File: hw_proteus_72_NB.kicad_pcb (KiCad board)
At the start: 2 copper layers, 154 x 159 mm, 130 parts, among them P1 1123038-2

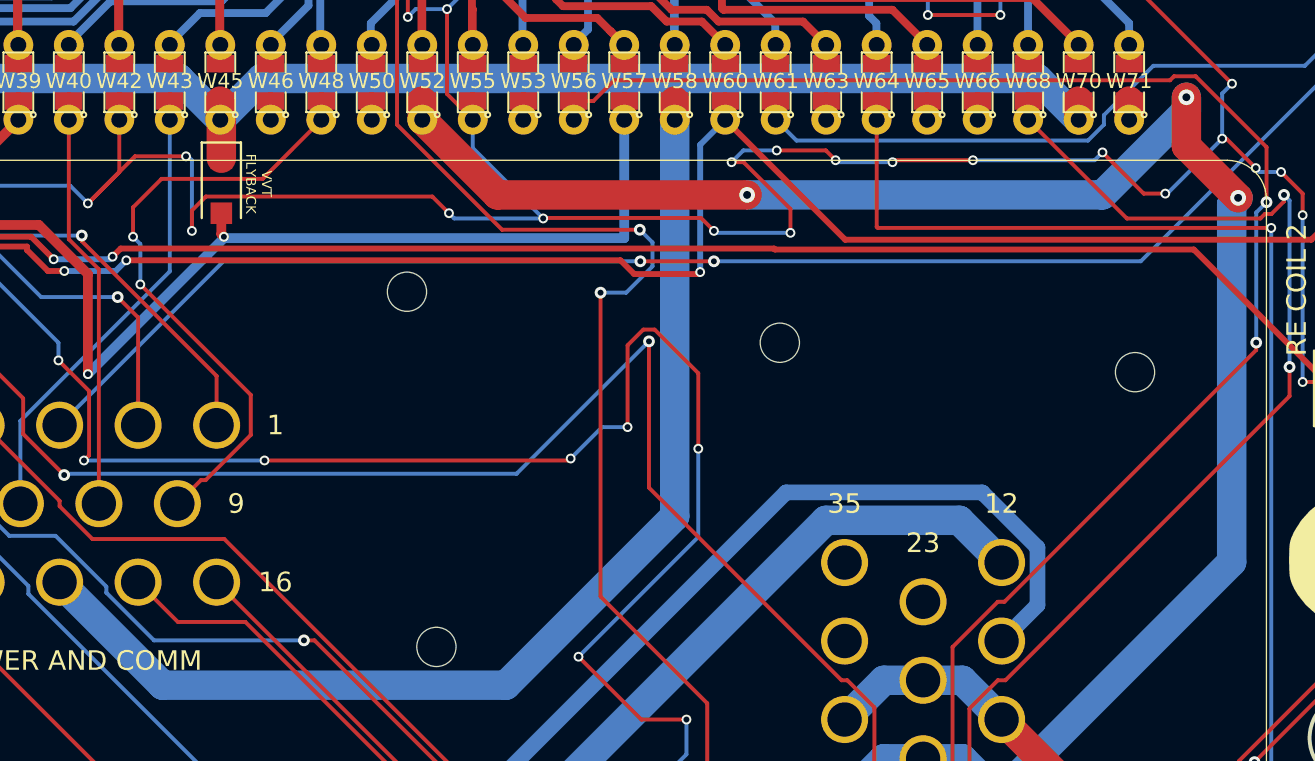
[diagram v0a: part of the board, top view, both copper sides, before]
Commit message: Added knock sensing connection
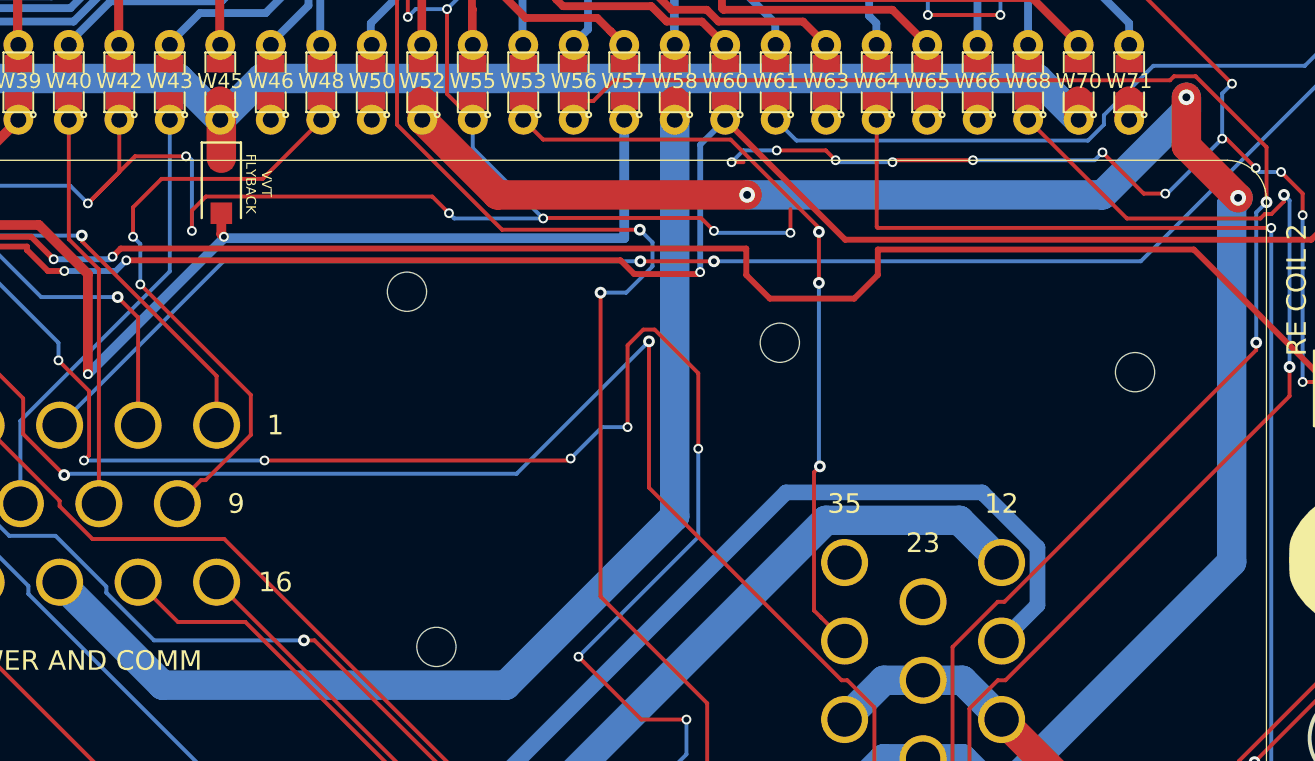
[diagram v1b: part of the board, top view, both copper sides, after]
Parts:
- renumbered e to D5
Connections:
- PROT2 pad 34: /KNOCK1 -> /KNOCK
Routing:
- net /KNOCK: track 0.95 -> 40.1 mm, vias 0 -> 3
- net /IGN4: track 266.7 -> 270.3 mm
- net GND: track 1283.1 -> 1279.7 mm

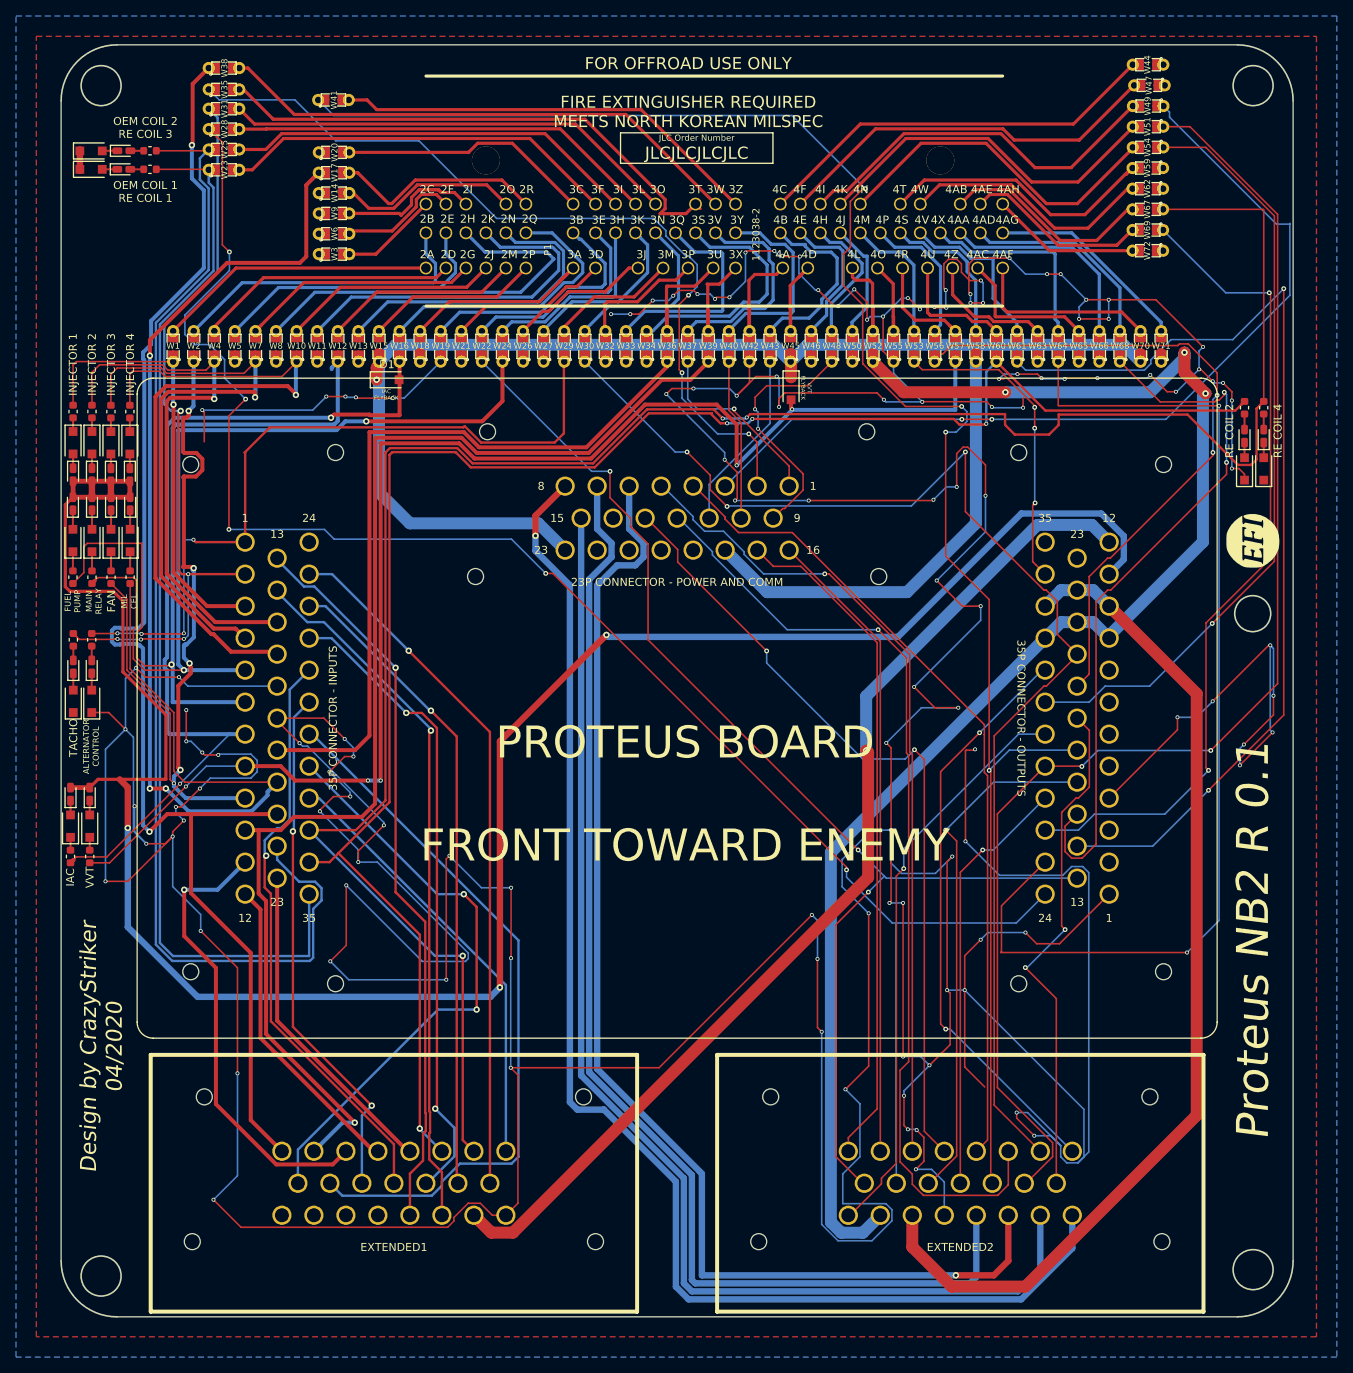
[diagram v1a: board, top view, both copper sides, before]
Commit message: Beefed up injector wires, as well as VVT and IAC low sides. Started the ground stitching process, TBC
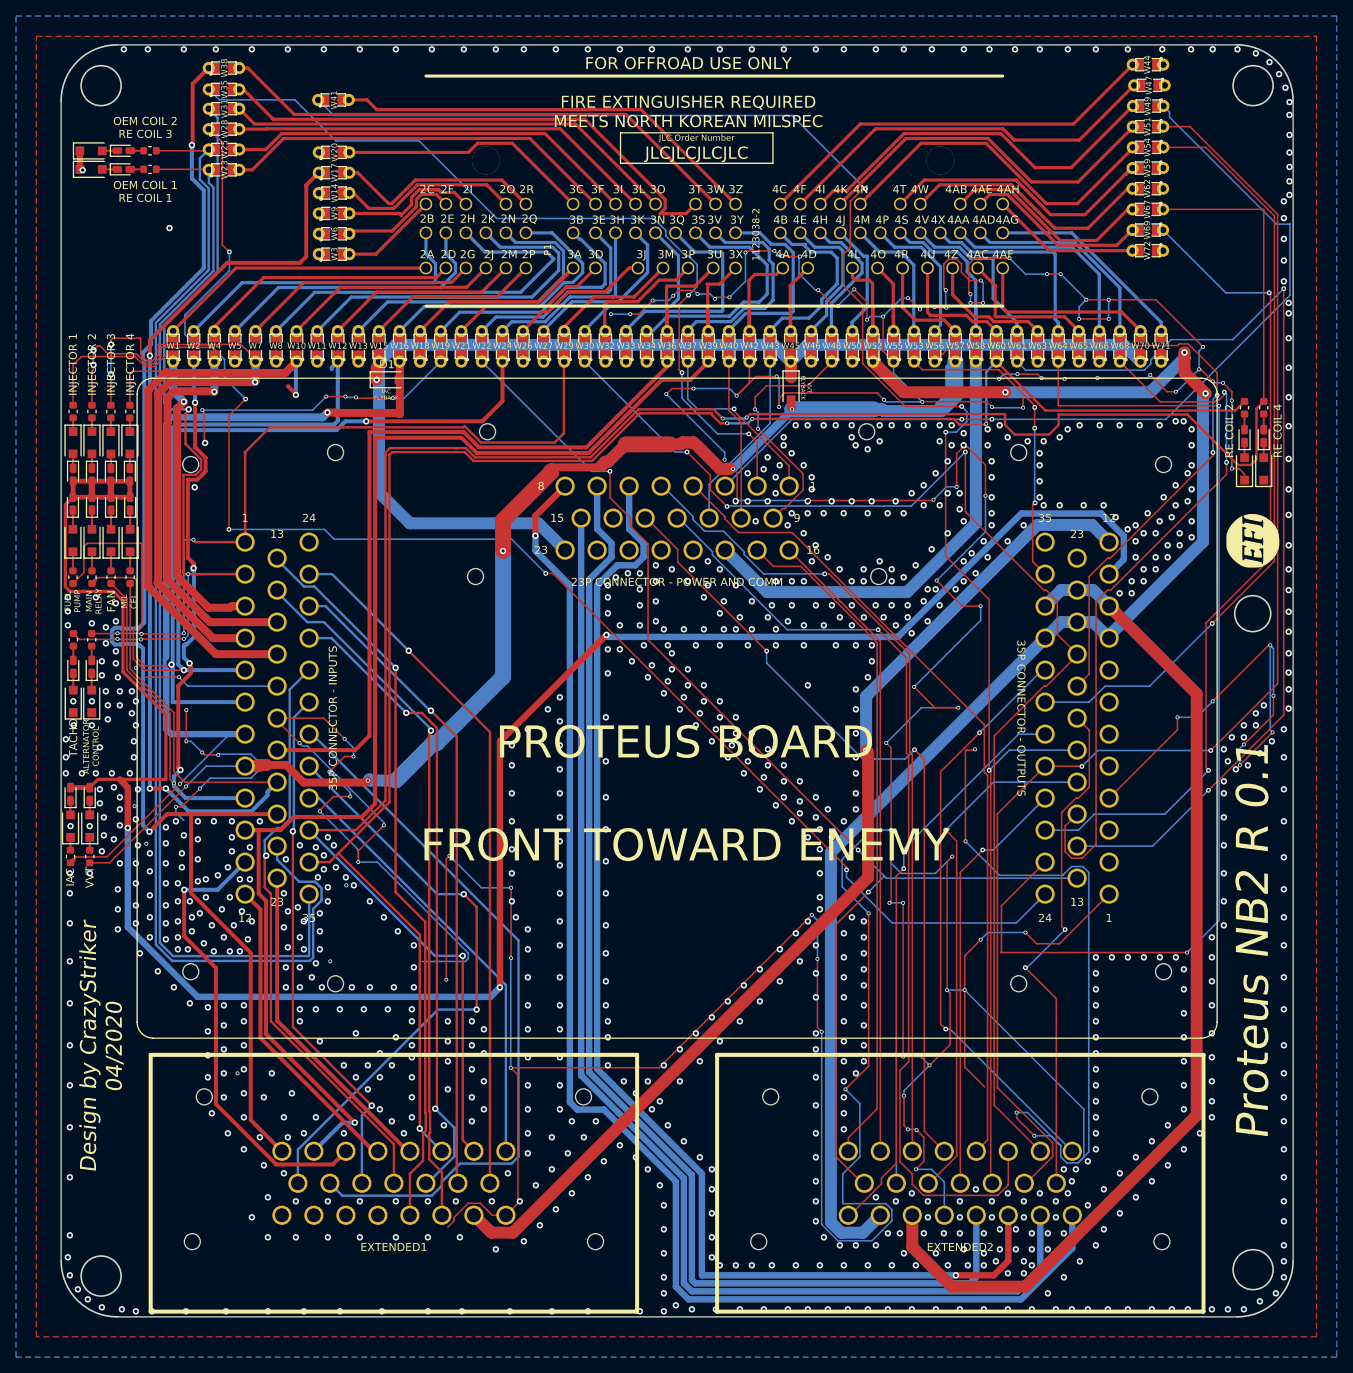
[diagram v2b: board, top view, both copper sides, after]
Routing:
- net GND: track 1279.7 -> 1084.9 mm, vias 132 -> 1073
- net /LS9: track 177.0 -> 210.3 mm
- net /IAC-: track 114.8 -> 134.0 mm
- net /INJ4: track 91.8 -> 80.1 mm
- net /INJ3: track 77.2 -> 84.7 mm, vias 1 -> 3
- net /INJ2: track 70.2 -> 75.4 mm, vias 1 -> 3
- net /FAN: track 100.1 -> 96.9 mm
- net /HS1: track 95.2 -> 98.2 mm
- net /INJ1: track 55.8 -> 58.1 mm
- net /IGN2: track 221.9 -> 221.3 mm

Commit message: switched LS and HS outputs to match hardware timers distribution. Added a 2k pulldown for the tach output"
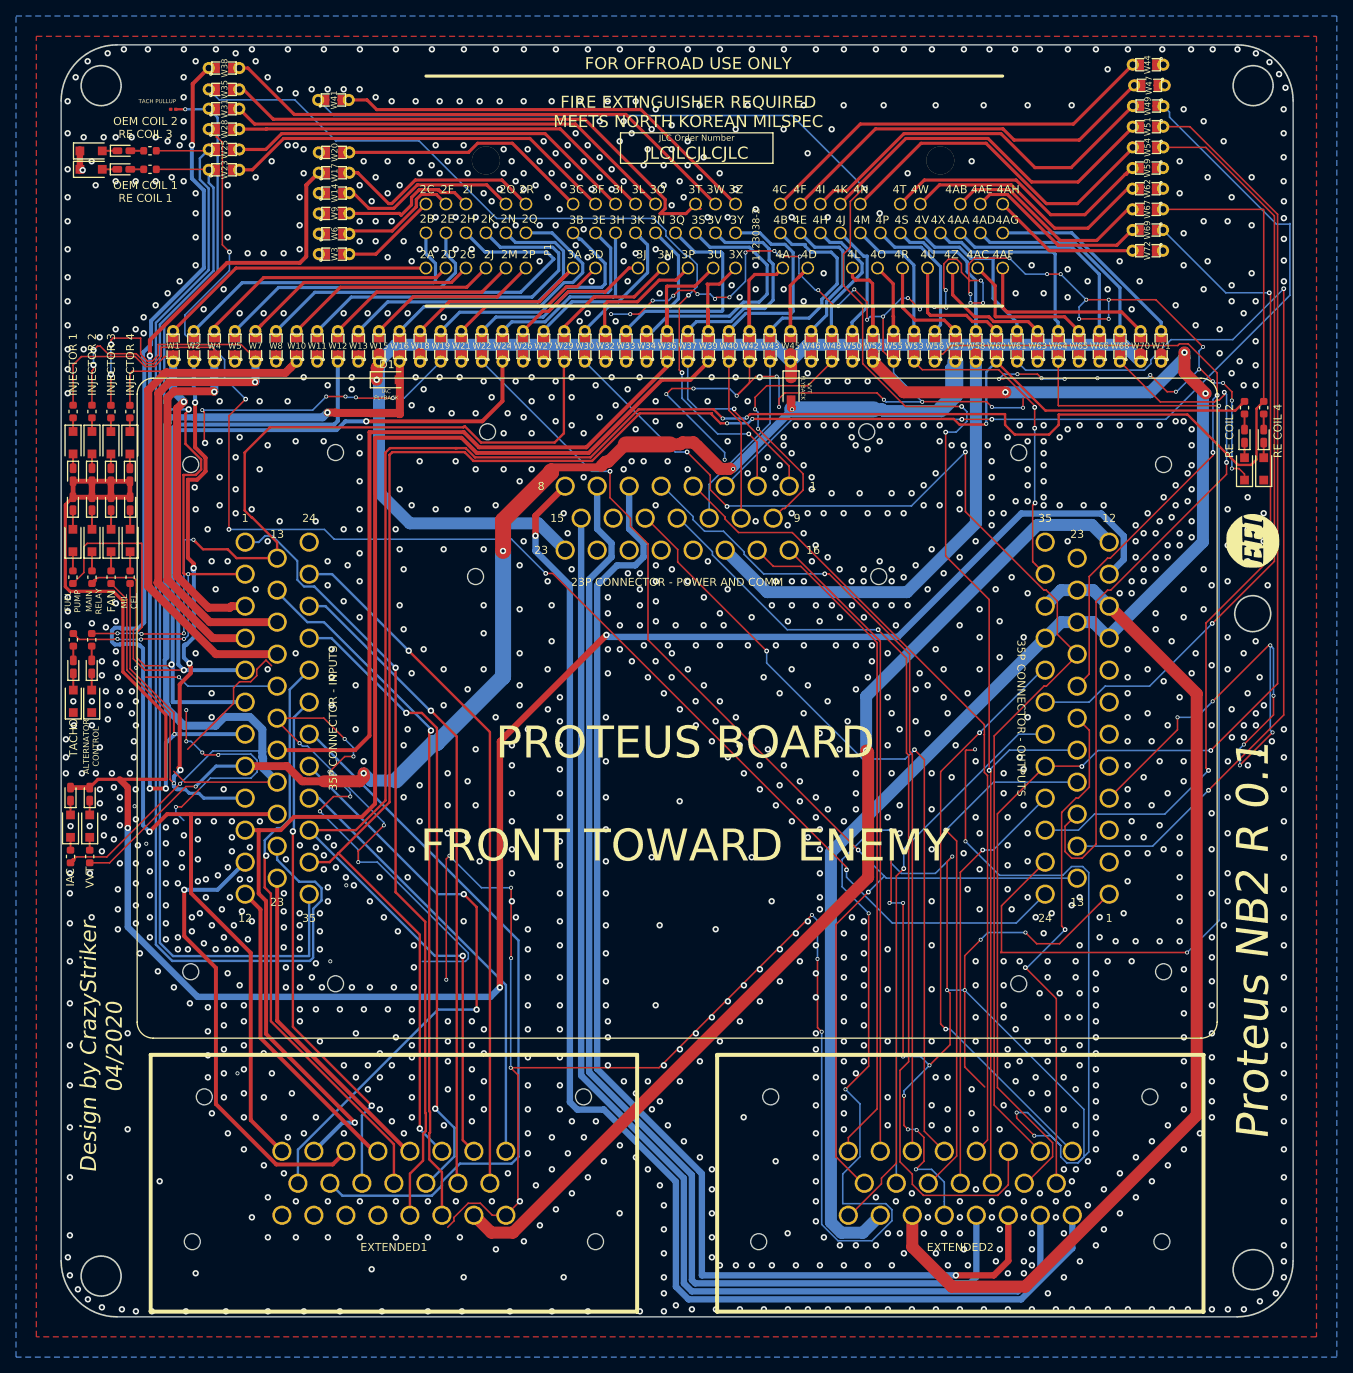
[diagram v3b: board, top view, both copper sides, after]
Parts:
- added R17: 1K, Resistor_SMD:R_0201_0603Metric, F.Cu at (118.2, 87.5)
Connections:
- EXTENDED1 pad 20: /HS3 -> /HS2
- PROT1 pad 1: /ALT_CONTROL -> /HS2
- PROT1 pad 13: /HS3 -> /ALT_CONTROL
- PROT1 pad 20: /LS10 -> /IAC-
- PROT1 pad 7: /IAC- -> /LS7
- R14 pad 2: /LS10 -> /LS7
- W17 pad 1: /LS10 -> /LS7
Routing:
- net /LS10: track 150.1 -> 0.00 mm, vias 3 -> 0
- net /LS7: track 0.00 -> 131.2 mm, vias 0 -> 4
- net GND: track 1084.9 -> 977.9 mm, vias 1073 -> 1614
- net /HS2: track 0.00 -> 98.6 mm, vias 0 -> 1
- net /HS3: track 91.4 -> 0.00 mm, vias 1 -> 0
- net /IAC-: track 134.0 -> 155.4 mm
- net (no net): track 0.00 -> 17.0 mm
- net /ALT_CONTROL: track 95.3 -> 104.1 mm
- net /INJ4: track 80.1 -> 74.3 mm, vias 1 -> 0
- net /HS1: track 98.2 -> 102.3 mm, vias 5 -> 6
- net /LS9: track 210.3 -> 208.3 mm
- net /FP_RELAY: track 106.0 -> 104.7 mm
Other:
- board text added: "TACH PULLUP"
